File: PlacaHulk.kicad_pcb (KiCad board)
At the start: 2 copper layers, 57.2 x 41.9 mm, 7 parts, among them J1 Conn_01x04, J2 DB25_Female, U1 MAX232

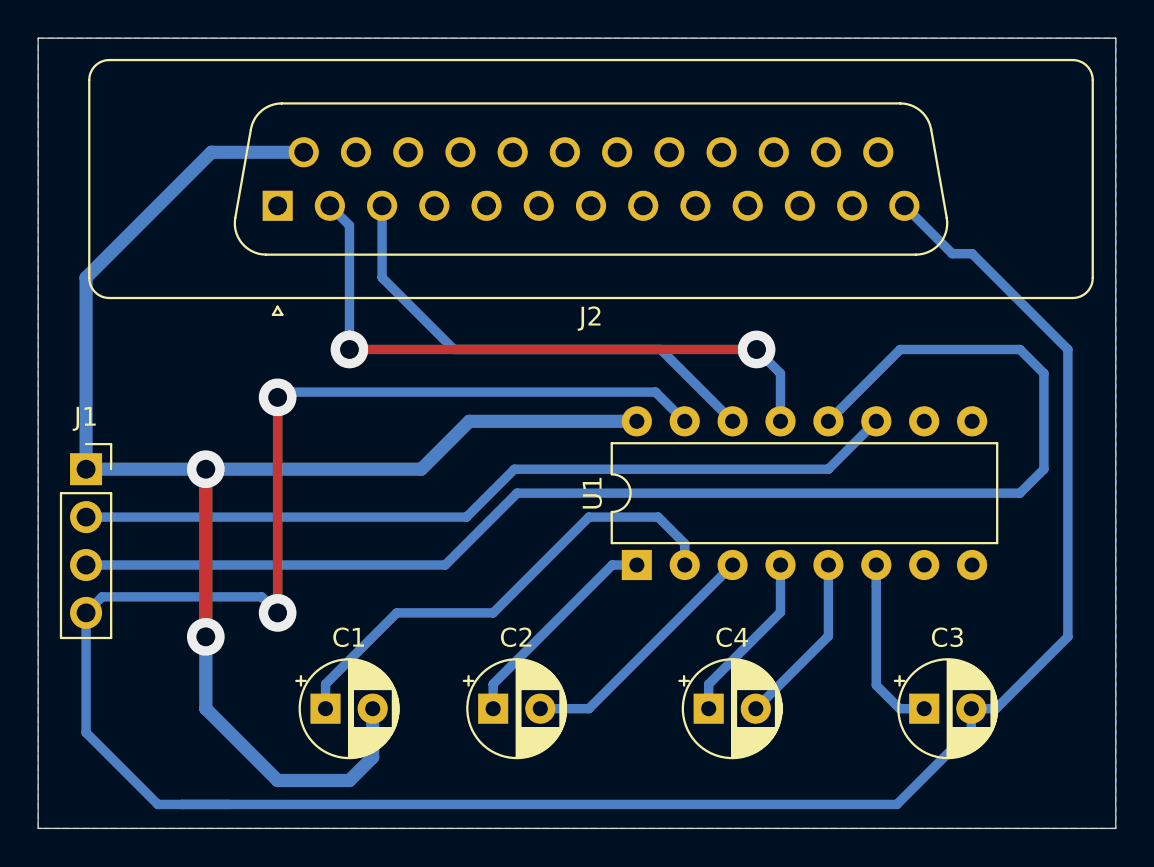
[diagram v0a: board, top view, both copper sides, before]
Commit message: Mudado os pinos usados e o layout da PCB.
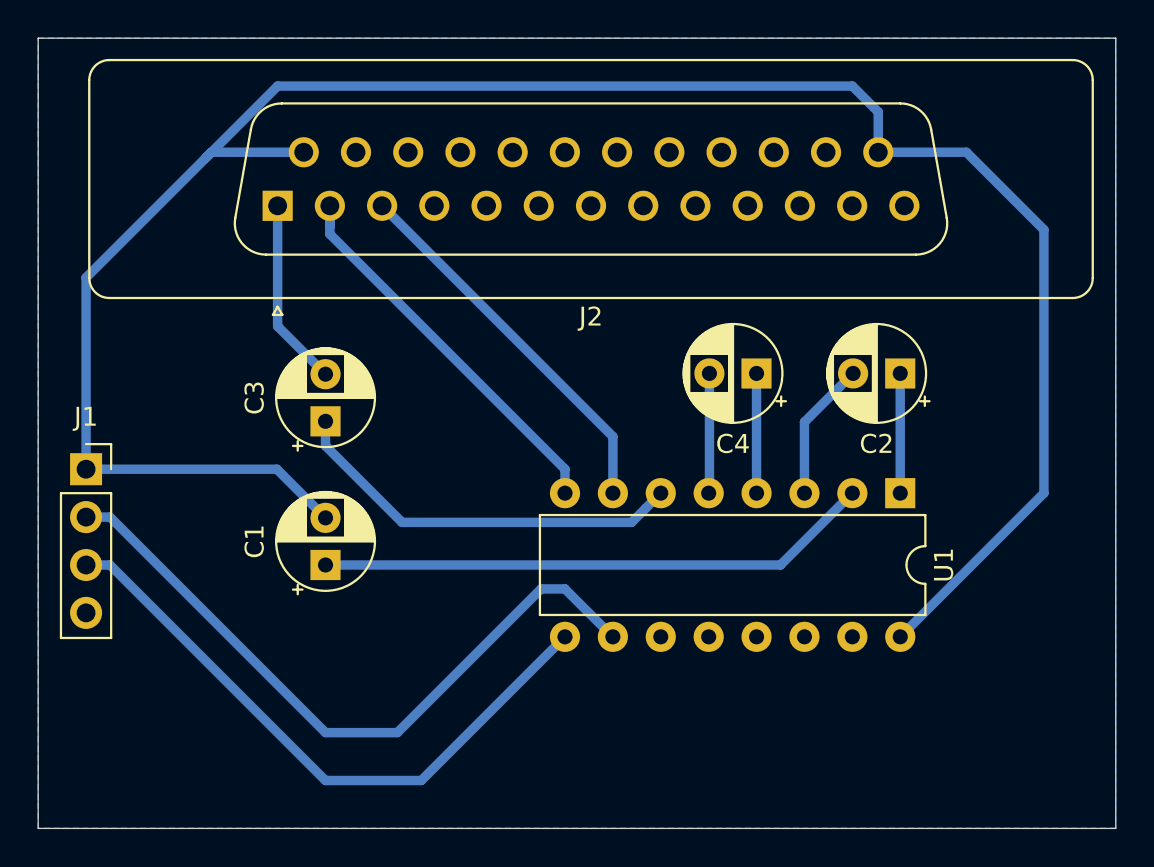
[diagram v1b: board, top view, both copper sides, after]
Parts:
- moved C3 35.2 mm to (116.8, 62.2), turned to 90 degrees
- moved C2 28.0 mm to (147.3, 59.7), turned to 180 degrees
- moved C4 18.0 mm to (139.7, 59.7), turned to 180 degrees
- moved U1 14.5 mm to (147.3, 66.0), turned to 270 degrees
- moved C1 7.62 mm to (116.8, 69.8), turned to 90 degrees
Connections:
- C1 pad 2: +5V -> +5C
- J1 pad 1: +5V -> +5C
- J2 pad 1: Net-(J2-Pad1) -> GND
- J2 pad 14: +5V -> +5C
- J2 pad 5: Net-(J2-Pad5) -> GND
- J2 pad 9: Net-(J2-Pad9) -> GND
- U1 pad 10: Net-(U1-Pad10) -> Net-(J1-Pad2)
- U1 pad 11: Net-(J1-Pad2) -> Net-(U1-Pad11)
- U1 pad 12: Net-(J1-Pad3) -> Net-(U1-Pad12)
- U1 pad 13: Net-(J2-Pad2) -> Net-(U1-Pad13)
- U1 pad 14: Net-(J2-Pad3) -> Net-(U1-Pad14)
- U1 pad 16: +5V -> +5C
- U1 pad 7: Net-(U1-Pad7) -> Net-(J2-Pad3)
- U1 pad 8: Net-(U1-Pad8) -> Net-(J2-Pad2)
- U1 pad 9: Net-(U1-Pad9) -> Net-(J1-Pad3)
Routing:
- net GND: track 138.6 -> 9.98 mm, vias 2 -> 0
- net +5C: track 0.00 -> 113.4 mm
- net +5V: track 80.9 -> 0.00 mm, vias 2 -> 0
- net Net-(J1-Pad3): track 71.5 -> 33.3 mm
- net Net-(J2-Pad2): track 34.0 -> 21.5 mm, vias 2 -> 0
- net Net-(C3-Pad1): track 9.43 -> 21.4 mm
- net Net-(J1-Pad2): track 44.0 -> 36.9 mm
- net Net-(C2-Pad2): track 13.4 -> 7.42 mm
- net Net-(J2-Pad3): track 25.6 -> 20.3 mm
- net Net-(C2-Pad1): track 11.5 -> 6.35 mm
- net Net-(C1-Pad1): track 25.8 -> 29.5 mm
- net Net-(C4-Pad2): track 9.21 -> 6.37 mm
- net Net-(C4-Pad1): track 9.20 -> 6.35 mm

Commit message: Refeito o layout da Placa com os conectores do encoder.
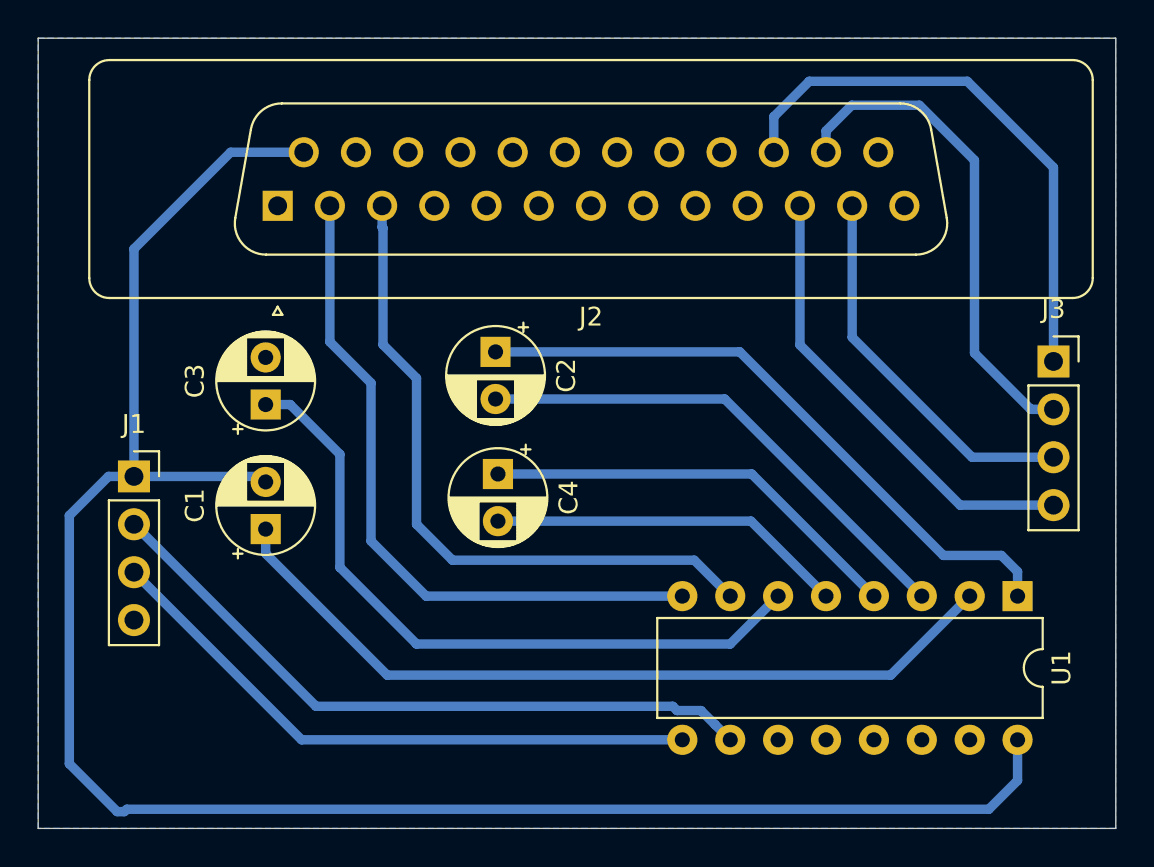
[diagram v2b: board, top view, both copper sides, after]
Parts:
- added J3: Conn_01x04, Connector_PinSocket_2.54mm:PinSocket_1x04_P2.54mm_Vertical, F.Cu at (155.4, 59.1)
- moved C2 21.5 mm to (125.9, 58.5), turned to 270 degrees
- moved C4 14.7 mm to (126.0, 65.0), turned to 270 degrees
- moved U1 8.28 mm to (153.5, 71.5)
- moved C1 3.70 mm to (113.7, 67.9)
- moved C3 3.30 mm to (113.7, 61.3)
- moved J1 2.57 mm to (106.7, 65.2)
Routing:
- net Net-(J2-Pad23): track 0.00 -> 29.7 mm
- net Net-(C2-Pad1): track 6.35 -> 33.8 mm
- net Net-(J2-Pad24): track 0.00 -> 26.4 mm
- net Net-(J2-Pad11): track 0.00 -> 24.3 mm
- net Net-(J2-Pad12): track 0.00 -> 20.3 mm
- net Net-(C2-Pad2): track 7.42 -> 26.9 mm
- net Net-(C4-Pad1): track 6.35 -> 22.6 mm
- net Net-(C3-Pad1): track 21.4 -> 37.0 mm
- net Net-(J2-Pad3): track 20.3 -> 35.9 mm
- net Net-(J2-Pad2): track 21.5 -> 36.4 mm
- net Net-(C1-Pad1): track 29.5 -> 43.0 mm
- net Net-(C4-Pad2): track 6.37 -> 19.0 mm
- net +5C: track 113.4 -> 101.9 mm
- net GND: track 9.98 -> 0.00 mm
- net Net-(J1-Pad2): track 36.9 -> 36.4 mm
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
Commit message: Aumentado a largura das trilhas.
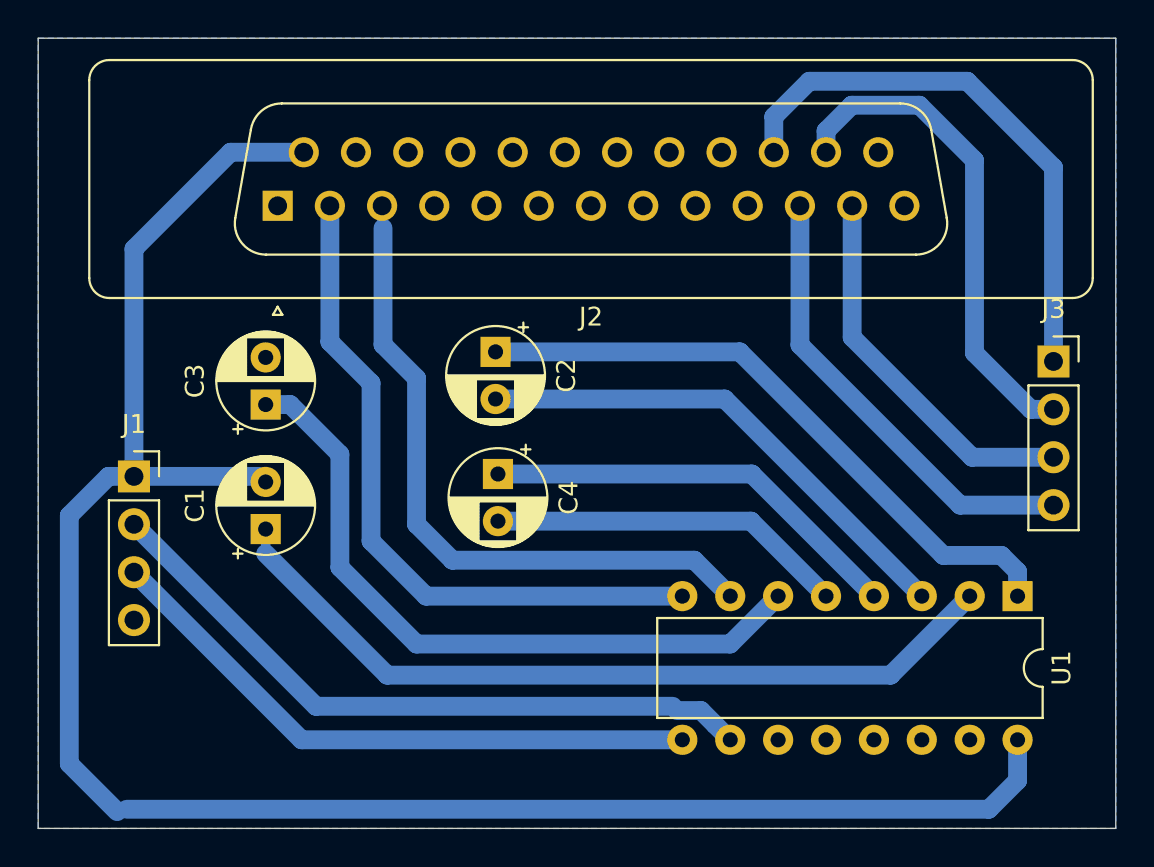
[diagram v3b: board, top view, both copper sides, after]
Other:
- net class Default: trace_width 0.5 -> 1
- net class Power: trace_width 0.7 -> 1.2
- rule via_min_size: 0.4 -> 0.7
